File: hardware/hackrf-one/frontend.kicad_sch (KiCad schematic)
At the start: 143 parts, among them J2 RF-SHIELD-FRAME, J3 RF-SHIELD-COVER, J4 MOUNTING_HOLE, J5 MOUNTING_HOLE, J6 MOUNTING_HOLE, J7 MOUNTING_HOLE, J8 MOUNTING_HOLE, J9 MOUNTING_HOLE, P13 GPO1, P19 GPO3, P27 MIXER_SDATA, P31 MIXER_SCLK, P32 MIXER_ENX, P33 MIXER_RESETX, P34 MIX_BYPASS, P35 !MIX_BYPASS, P4 ANTENNA, P43 RX, P44 HP, P45 LP, P46 TX_MIX_BP, P47 RX_MIX_BP, P48 TX_AMP, P49 RX_AMP, P50 AMP_BYPASS, P51 !TX_AMP_PWR, P52 !RX_AMP_PWR, P6 GPO4, Q1 MOSFET_P, Q2 MOSFET_P, Q4 MOSFET_P, T1 MIX_IN_BALUN, T2 MIX_OUT_BALUN, U1 SKY13453, U10 SKY13453, U11 SKY13453, U12 SKY13317, U13 MGA-81563, U14 SKY13317, U2 SKY13453, U25 MGA-81563, U3 RX_LOWPASS_FILTER, U4 RFFC5072, U5 SKY13453, U6 SKY13453, U7 SKY13453, U8 RX_HIGHPASS_FILTER, U9 SKY13317

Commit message: HackRF One: update 100 nF capacitor part selection
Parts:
- C166, C17, C18, C20, C23, C25, C28, C31, C44, C46, C49, C50, C58, C59, C61, C62, C64, C9: Manufacturer Murata -> Samsung; Part Number GRM155R61A104KA01D -> CL05A104KA5NNNC

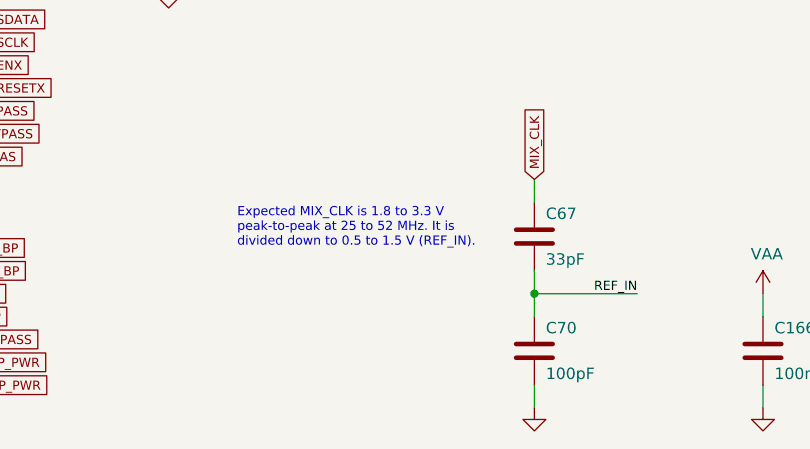
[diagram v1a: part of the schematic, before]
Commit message: HackRF One: update clock termination passives
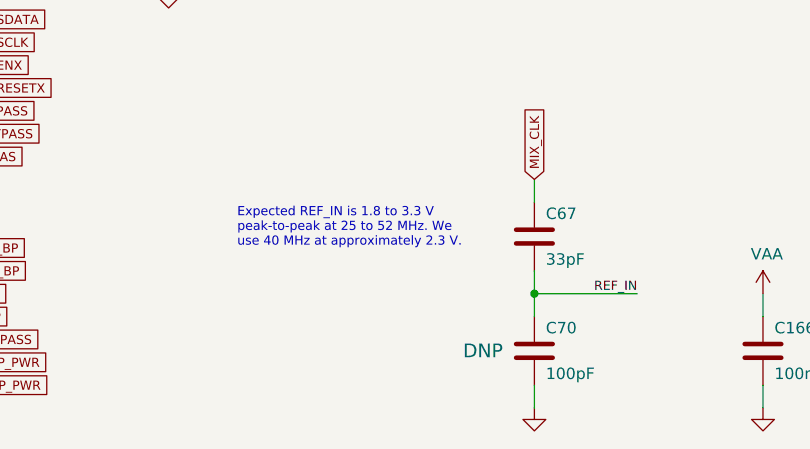
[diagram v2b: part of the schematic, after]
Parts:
- C70: DNP (none) -> DNP
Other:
- note added: "Expected REF_IN is 1.8 to 3.3 V peak-to-peak at 25 to 52 MHz. We use 40 MHz at approximately 2.3 V."
- note removed: "Expected MIX_CLK is 1.8 to 3.3 V peak-to-peak at 25 to 52 MHz. It is divided down to 0.5 to 1.5 V (REF_IN)."
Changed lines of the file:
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@@
     (effects (font (size 1.016 1.016)) (justify left bottom))
   )
-  (text "Expected MIX_CLK is 1.8 to 3.3 V\npeak-to-peak at 25 to 52 MHz. It is\ndivided down to 0.5 to 1.5 V (REF_IN)."
+  (text "Expected REF_IN is 1.8 to 3.3 V\npeak-to-peak at 25 to 52 MHz. We\nuse 40 MHz at approximately 2.3 V."
     (at 127 243.84 0)
     (effects (font (size 1.016 1.016)) (justify left bottom))
@@
       (effects (font (size 1.524 1.524)) hide)
     )
+    (property "DNP" "DNP" (id 7) (at 154.305 255.27 0)
+      (effects (font (size 1.524 1.524)))
+    )
     (pin "1")

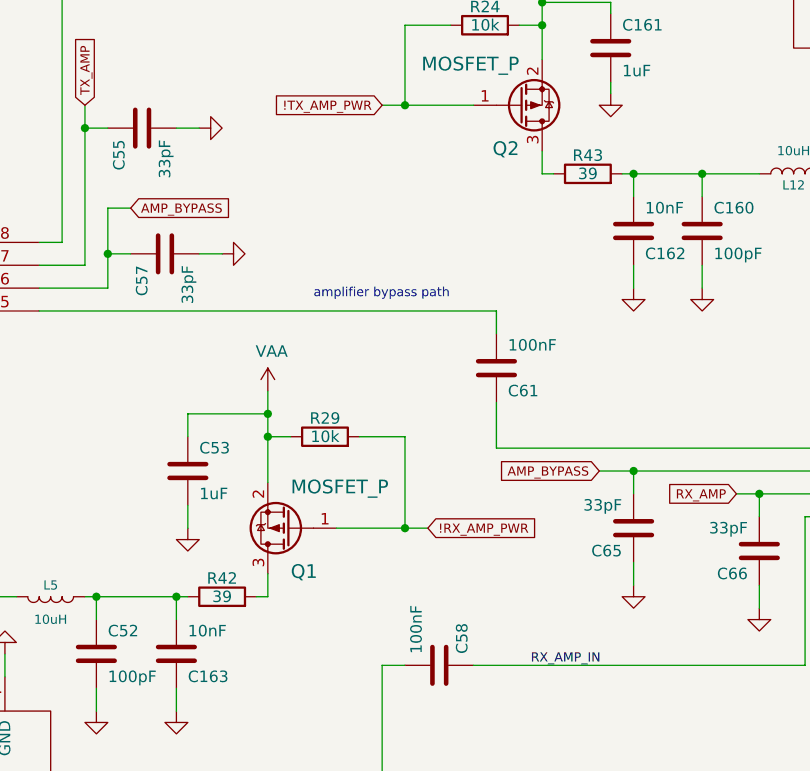
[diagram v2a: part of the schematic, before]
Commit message: HackRF One: update RF amplifier series resistance
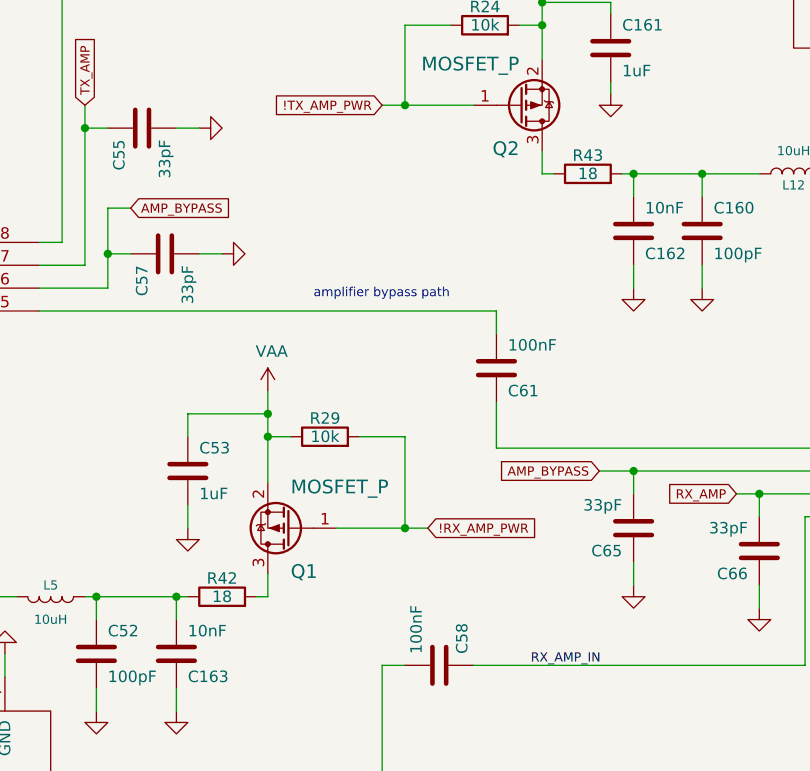
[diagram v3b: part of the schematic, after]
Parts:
- R42, R43: value 39 -> 18; Manufacturer Stackpole -> Yageo; Part Number RMCF0402JT39R0 -> RC0402JR-0718RL
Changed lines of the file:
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@@
     (in_bom yes) (on_board yes)
     (property "Reference" "R43" (id 0) (at 307.34 174.498 90))
-    (property "Value" "39" (id 1) (at 307.34 176.53 90))
+    (property "Value" "18" (id 1) (at 307.34 176.53 90))
     (property "Footprint" "hackrf:GSG-0402" (id 2) (at 307.34 176.53 0)
       (effects (font (size 1.524 1.524)) hide)
@@
       (effects (font (size 1.524 1.524)) hide)
     )
-    (property "Manufacturer" "Stackpole" (id 4) (at 307.34 176.53 0)
+    (property "Manufacturer" "Yageo" (id 4) (at 307.34 176.53 0)
       (effects (font (size 1.524 1.524)) hide)
     )
-    (property "Part Number" "RMCF0402JT39R0" (id 5) (at 307.34 176.53 0)
+    (property "Part Number" "RC0402JR-0718RL" (id 5) (at 307.34 176.53 0)
       (effects (font (size 1.524 1.524)) hide)
     )
-    (property "Description" "RES 39 OHM 1/16W 5% 0402 SMD" (id 6) (at 307.34 176.53 0)
+    (property "Description" "RES 18 OHM 5% 1/16W 0402" (id 6) (at 307.34 176.53 0)
       (effects (font (size 1.524 1.524)) hide)
     )
@@
     (in_bom yes) (on_board yes)
     (property "Reference" "R42" (id 0) (at 266.7 221.488 90))
-    (property "Value" "39" (id 1) (at 266.7 223.52 90))
+    (property "Value" "18" (id 1) (at 266.7 223.52 90))
     (property "Footprint" "hackrf:GSG-0402" (id 2) (at 266.7 223.52 0)
       (effects (font (size 1.524 1.524)) hide)
@@
       (effects (font (size 1.524 1.524)) hide)
     )
-    (property "Manufacturer" "Stackpole" (id 4) (at 266.7 223.52 0)
+    (property "Manufacturer" "Yageo" (id 4) (at 266.7 223.52 0)
       (effects (font (size 1.524 1.524)) hide)
     )
-    (property "Part Number" "RMCF0402JT39R0" (id 5) (at 266.7 223.52 0)
+    (property "Part Number" "RC0402JR-0718RL" (id 5) (at 266.7 223.52 0)
       (effects (font (size 1.524 1.524)) hide)
     )
-    (property "Description" "RES 39 OHM 1/16W 5% 0402 SMD" (id 6) (at 266.7 223.52 0)
+    (property "Description" "RES 18 OHM 5% 1/16W 0402" (id 6) (at 266.7 223.52 0)
       (effects (font (size 1.524 1.524)) hide)
     )

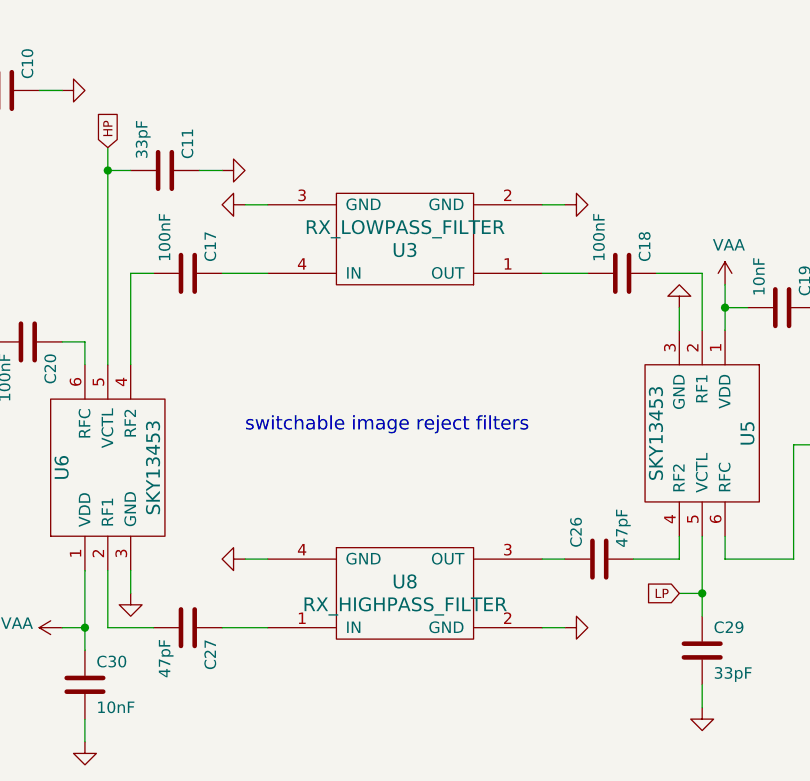
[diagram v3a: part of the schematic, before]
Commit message: HackRF One: clean up
- silkscreen
- fabrication attributes
- dates
- copyright
- README
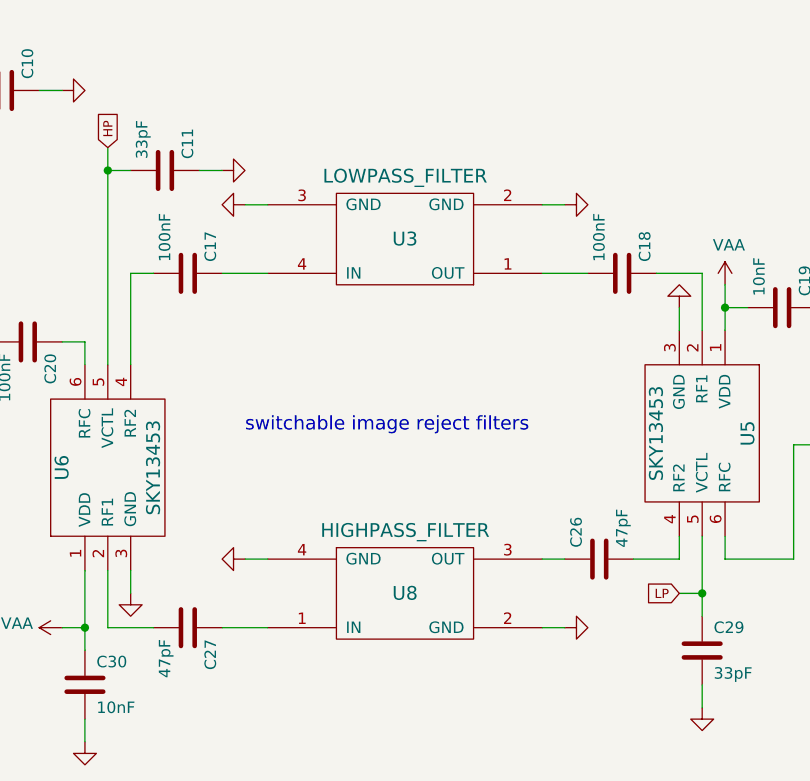
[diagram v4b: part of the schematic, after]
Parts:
- U3: value RX_LOWPASS_FILTER -> LOWPASS_FILTER
- U8: value RX_HIGHPASS_FILTER -> HIGHPASS_FILTER
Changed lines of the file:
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@@
   (title_block
     (title "HackRF One")
-    (date "2022-08-29")
+    (date "2022-10-30")
     (rev "r9")
     (company "Copyright 2012-2022 Great Scott Gadgets")
-    (comment 1 "Michael Ossmann")
-    (comment 2 "Licensed under the CERN-OHL-P v2")
+    (comment 1 "Licensed under the CERN-OHL-P v2")
   )
   (junction (at 111.76 121.92) (diameter 0) (color 0 0 0 0)
@@
   (symbol (lib_id "hackrf:FIL-DEA") (at 289.56 97.79 0) (unit 1)
     (in_bom yes) (on_board yes)
-    (property "Reference" "U8" (id 0) (at 289.56 96.52 0)
+    (property "Reference" "U8" (id 0) (at 289.56 97.79 0)
       (effects (font (size 1.524 1.524)))
     )
-    (property "Value" "RX_HIGHPASS_FILTER" (id 1) (at 289.56 99.06 0)
+    (property "Value" "HIGHPASS_FILTER" (id 1) (at 289.56 90.805 0)
       (effects (font (size 1.524 1.524)))
     )
@@
   (symbol (lib_id "hackrf:FIL-LP0603") (at 289.56 58.42 180) (unit 1)
     (in_bom yes) (on_board yes)
-    (property "Reference" "U3" (id 0) (at 289.56 59.69 0)
+    (property "Reference" "U3" (id 0) (at 289.56 58.42 0)
       (effects (font (size 1.524 1.524)))
     )
-    (property "Value" "RX_LOWPASS_FILTER" (id 1) (at 289.56 57.15 0)
+    (property "Value" "LOWPASS_FILTER" (id 1) (at 289.56 51.435 0)
       (effects (font (size 1.524 1.524)))
     )
